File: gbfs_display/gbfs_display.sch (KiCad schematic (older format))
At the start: 9 parts, among them U1 esp8266_thing_dev

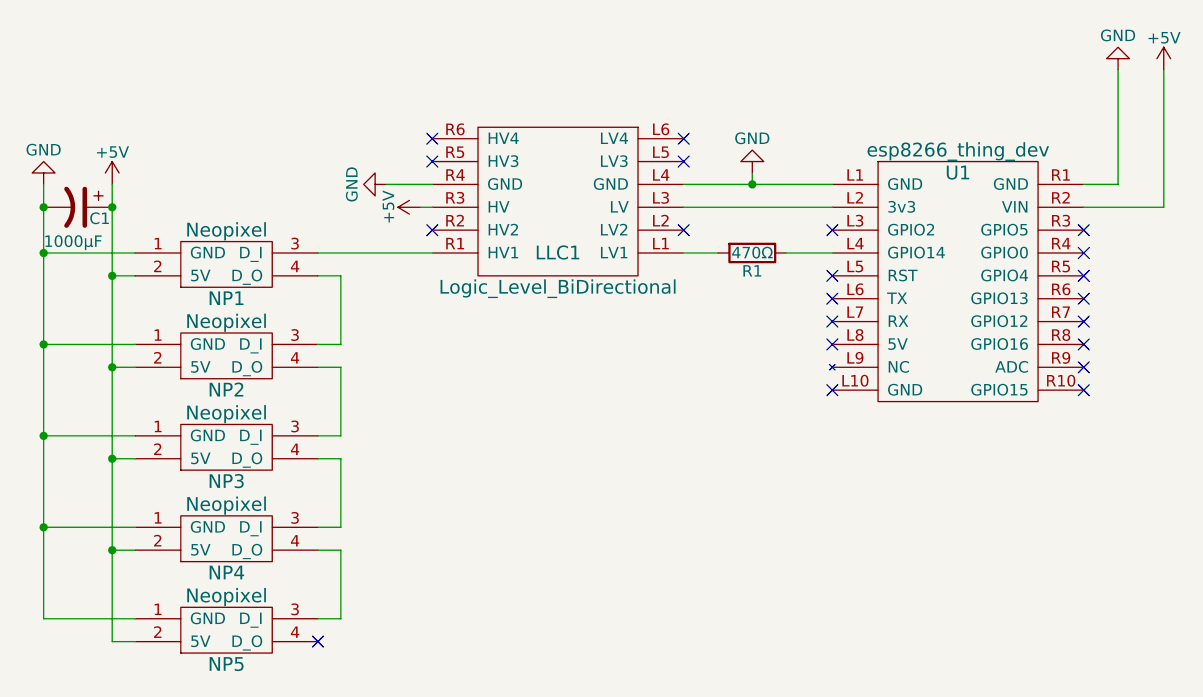
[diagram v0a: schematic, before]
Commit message: Remove neopixels and add footprints
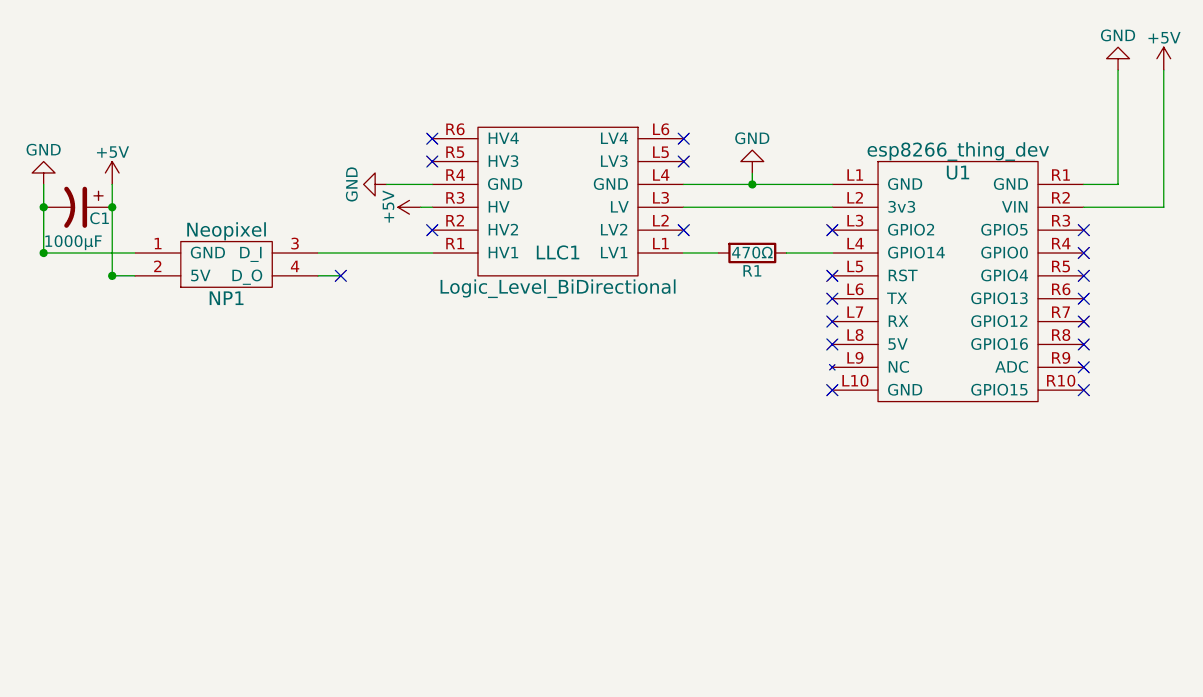
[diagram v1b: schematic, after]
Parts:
- removed NP2, NP3, NP4, NP5: Neopixel, symbol Neopixel
- C1: footprint (none) -> Capacitors_ThroughHole:CP_Radial_D10.0mm_P5.00mm
- LLC1: footprint (none) -> gbfs_display:Logic_Level_Bidirectional
- NP1: footprint (none) -> Wire_Pads:SolderWirePad_3x_2-5mmDrill
- R1: footprint (none) -> Resistors_ThroughHole:R_Axial_DIN0204_L3.6mm_D1.6mm_P5.08mm_Horizontal
- U1: footprint (none) -> gbfs_display:esp8266_thing
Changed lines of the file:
@@
 F 0 "U1" H 6050 3350 60  0000 C CNN
 F 1 "esp8266_thing_dev" H 6050 3450 60  0000 C CNN
-F 2 "" H 6050 2750 60  0001 C CNN
+F 2 "gbfs_display:esp8266_thing" H 6050 2750 60  0001 C CNN
 F 3 "" H 6050 2750 60  0001 C CNN
 	1    6050 2850
@@
 F 0 "LLC1" H 4300 2700 60  0000 C CNN
 F 1 "Logic_Level_BiDirectional" H 4300 2850 60  0000 C CNN
-F 2 "" H 4300 2150 60  0001 C CNN
+F 2 "gbfs_display:Logic_Level_Bidirectional" H 4300 2150 60  0001 C CNN
 F 3 "" H 4300 2150 60  0001 C CNN
 	1    4300 2250
@@
 F 0 "NP1" H 2850 3400 60  0000 C CNN
 F 1 "Neopixel" H 2850 3700 60  0000 C CNN
-F 2 "" H 2850 3050 60  0001 C CNN
+F 2 "Wire_Pads:SolderWirePad_3x_2-5mmDrill" H 2850 3050 60  0001 C CNN
 F 3 "" H 2850 3050 60  0001 C CNN
 	1    2850 3150
 	1    0    0    -1
 $EndComp
-$Comp
-L Neopixel NP2
-U 1 1 5A077CB3
-P 2850 3550
-F 0 "NP2" H 2850 3800 60  0000 C CNN
-F 1 "Neopixel" H 2850 4100 60  0000 C CNN
-F 2 "" H 2850 3450 60  0001 C CNN
-F 3 "" H 2850 3450 60  0001 C CNN
-	1    2850 3550
-	1    0    0    -1
-$EndComp
-$Comp
-L Neopixel NP3
-U 1 1 5A077CD9
-P 2850 3950
-F 0 "NP3" H 2850 4200 60  0000 C CNN
-F 1 "Neopixel" H 2850 4500 60  0000 C CNN
-F 2 "" H 2850 3850 60  0001 C CNN
-F 3 "" H 2850 3850 60  0001 C CNN
-	1    2850 3950
-	1    0    0    -1
-$EndComp
-$Comp
-L Neopixel NP4
-U 1 1 5A077D04
-P 2850 4350
-F 0 "NP4" H 2850 4600 60  0000 C CNN
-F 1 "Neopixel" H 2850 4900 60  0000 C CNN
-F 2 "" H 2850 4250 60  0001 C CNN
-F 3 "" H 2850 4250 60  0001 C CNN
-	1    2850 4350
-	1    0    0    -1
-$EndComp
-$Comp
-L Neopixel NP5
-U 1 1 5A077D34
-P 2850 4750
-F 0 "NP5" H 2850 5000 60  0000 C CNN
-F 1 "Neopixel" H 2850 5300 60  0000 C CNN
-F 2 "" H 2850 4650 60  0001 C CNN
-F 3 "" H 2850 4650 60  0001 C CNN
-	1    2850 4750
-	1    0    0    -1
-$EndComp
 Wire Wire Line
 	3250 2800 3350 2800
-Wire Wire Line
-	3350 2800 3350 3100
-Wire Wire Line
-	3350 3100 3250 3100
-Wire Wire Line
-	3250 3200 3350 3200
-Wire Wire Line
-	3350 3200 3350 3500
-Wire Wire Line
-	3350 3500 3250 3500
-Wire Wire Line
-	3250 3600 3350 3600
-Wire Wire Line
-	3350 3600 3350 3900
-Wire Wire Line
-	3350 3900 3250 3900
-Wire Wire Line
-	3250 4000 3350 4000
-Wire Wire Line
-	3350 4000 3350 4300
-Wire Wire Line
-	3350 4300 3250 4300
-Wire Wire Line
-	2350 3200 2450 3200
-Wire Wire Line
-	2350 3600 2450 3600
-Connection ~ 2350 3200
-Wire Wire Line
-	2350 4000 2450 4000
-Connection ~ 2350 3600
-Wire Wire Line
-	2350 4400 2450 4400
-Connection ~ 2350 4000
 Connection ~ 2350 2800
 Wire Wire Line
@@
 Wire Wire Line
 	3750 2400 3550 2400
-NoConn ~ 3250 4400
 NoConn ~ 6600 2600
 NoConn ~ 6600 2700
@@
 Wire Wire Line
 	3700 2500 3750 2500
-Wire Wire Line
-	2350 2400 2350 4400
 $Comp
 L +5V #PWR07
@@
 F 0 "C1" V 2250 2550 50  0000 L CNN
 F 1 "1000µF" V 2350 2350 50  0000 L CNN
-F 2 "" H 2200 2500 50  0000 C CNN
+F 2 "Capacitors_ThroughHole:CP_Radial_D10.0mm_P5.00mm" H 2200 2500 50  0001 C CNN
 F 3 "" H 2200 2500 50  0000 C CNN
 	1    2200 2500
 	0    1    1    0
 $EndComp
-Wire Wire Line
-	2050 2400 2050 4300
-Wire Wire Line
-	2050 4300 2450 4300
-Wire Wire Line
-	2450 3900 2050 3900
-Connection ~ 2050 3900
-Wire Wire Line
-	2450 3500 2050 3500
-Connection ~ 2050 3500
-Wire Wire Line
-	2450 3100 2050 3100
-Connection ~ 2050 3100
 Wire Wire Line
 	2450 2700 2050 2700
@@
 F 0 "R1" V 5230 2700 50  0000 C CNN
 F 1 "470Ω" V 5150 2700 50  0000 C CNN
-F 2 "" V 5080 2700 50  0000 C CNN
+F 2 "Resistors_ThroughHole:R_Axial_DIN0204_L3.6mm_D1.6mm_P5.08mm_Horizontal" V 5080 2700 50  0001 C CNN
 F 3 "" H 5150 2700 50  0000 C CNN
 	1    5150 2700
@@
 Wire Wire Line
 	5500 2500 4850 2500
+NoConn ~ 3350 2800
+Wire Wire Line
+	2350 2800 2350 2400
+Wire Wire Line
+	2050 2700 2050 2400
 $EndSCHEMATC

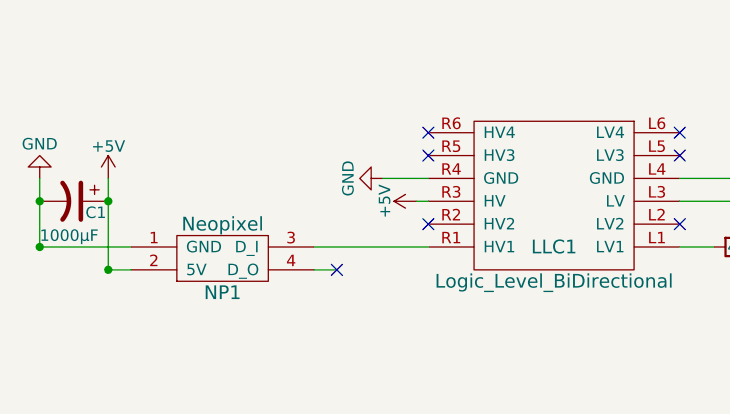
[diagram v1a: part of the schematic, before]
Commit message: New Footprint for the cable
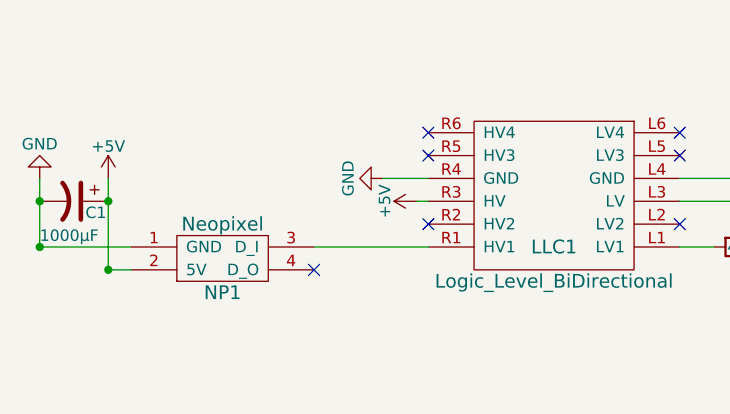
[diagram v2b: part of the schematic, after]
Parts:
- NP1: footprint Wire_Pads:SolderWirePad_3x_2-5mmDrill -> gbfs_display:NeoConnect_SolderWirePad_3x_2-5mmDrill
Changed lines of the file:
@@
 F 0 "NP1" H 2850 3400 60  0000 C CNN
 F 1 "Neopixel" H 2850 3700 60  0000 C CNN
-F 2 "Wire_Pads:SolderWirePad_3x_2-5mmDrill" H 2850 3050 60  0001 C CNN
+F 2 "gbfs_display:NeoConnect_SolderWirePad_3x_2-5mmDrill" H 2850 3050 60  0001 C CNN
 F 3 "" H 2850 3050 60  0001 C CNN
 	1    2850 3150
 	1    0    0    -1
 $EndComp
-Wire Wire Line
-	3250 2800 3350 2800
-Connection ~ 2350 2800
-Wire Wire Line
-	3750 2700 3250 2700
-Wire Wire Line
-	6750 1900 6750 2400
-Wire Wire Line
-	6750 2400 6600 2400
-Wire Wire Line
-	3750 2400 3550 2400
 NoConn ~ 6600 2600
 NoConn ~ 6600 2700
@@
 	-1   0    0    1
 $EndComp
-Connection ~ 5150 2400
-Wire Wire Line
-	6600 2500 6950 2500
-Wire Wire Line
-	6950 2500 6950 1900
-Wire Wire Line
-	2450 2800 2350 2800
-Wire Wire Line
-	3700 2500 3750 2500
 $Comp
 L +5V #PWR07
@@
 	0    1    1    0
 $EndComp
-Wire Wire Line
-	2450 2700 2050 2700
-Connection ~ 2050 2700
-Connection ~ 2050 2500
-Connection ~ 2350 2500
 $Comp
 L R R1
@@
 $EndComp
 Wire Wire Line
-	5500 2400 4850 2400
+	2050 2700 2050 2400
+Wire Wire Line
+	2350 2800 2350 2400
+Wire Wire Line
+	5500 2500 4850 2500
+Wire Wire Line
+	5000 2700 4850 2700
+Wire Wire Line
+	5500 2700 5300 2700
 Wire Wire Line
 	5150 2350 5150 2400
 Wire Wire Line
-	5500 2700 5300 2700
+	5500 2400 4850 2400
+Connection ~ 2350 2500
+Connection ~ 2050 2500
+Connection ~ 2050 2700
 Wire Wire Line
-	5000 2700 4850 2700
+	2450 2700 2050 2700
 Wire Wire Line
-	5500 2500 4850 2500
-NoConn ~ 3350 2800
+	3700 2500 3750 2500
 Wire Wire Line
-	2350 2800 2350 2400
+	2450 2800 2350 2800
 Wire Wire Line
-	2050 2700 2050 2400
+	6950 2500 6950 1900
+Wire Wire Line
+	6600 2500 6950 2500
+Connection ~ 5150 2400
+Wire Wire Line
+	3750 2400 3550 2400
+Wire Wire Line
+	6750 2400 6600 2400
+Wire Wire Line
+	6750 1900 6750 2400
+Wire Wire Line
+	3750 2700 3250 2700
+Connection ~ 2350 2800
+NoConn ~ 3250 2800
 $EndSCHEMATC

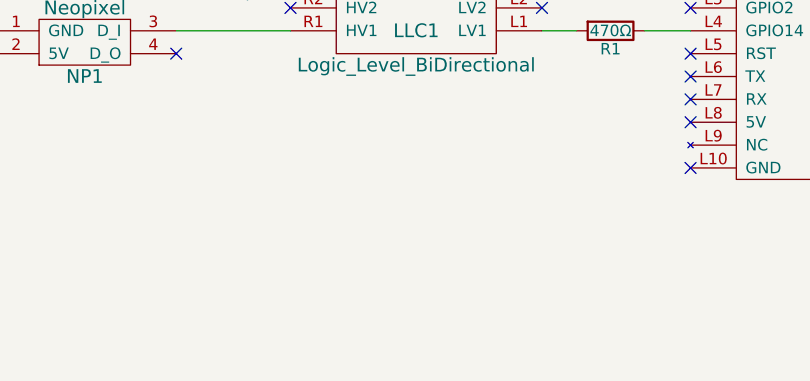
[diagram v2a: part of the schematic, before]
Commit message: Add power to schematic
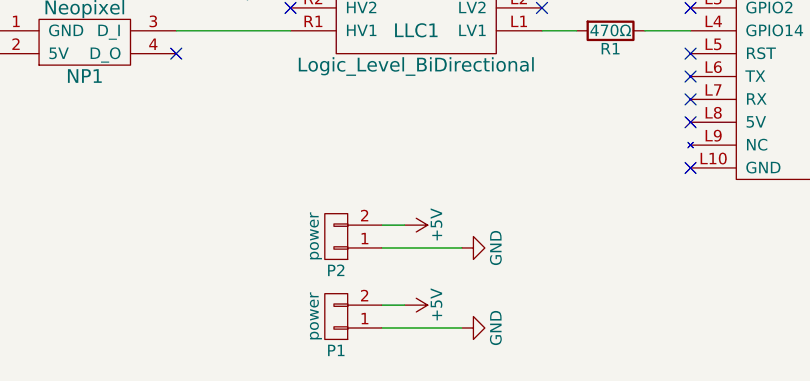
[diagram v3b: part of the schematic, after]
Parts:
- added P1, P2: power, symbol aux_conn
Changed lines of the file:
@@
 LIBS:valves
 LIBS:gbfs_lib
+LIBS:gbfs_display-cache
 EELAYER 25 0
 EELAYER END
@@
 Connection ~ 2350 2800
 NoConn ~ 3250 2800
+$Comp
+L aux_conn P1
+U 1 1 5A07C2BB
+P 3950 3950
+F 0 "P1" H 3950 4100 50  0000 C CNN
+F 1 "power" V 4050 3950 50  0000 C CNN
+F 2 "" H 3950 3950 50  0000 C CNN
+F 3 "" H 3950 3950 50  0000 C CNN
+	1    3950 3950
+	-1   0    0    1
+$EndComp
+$Comp
+L +5V #PWR?
+U 1 1 5A07C408
+P 4250 3900
+F 0 "#PWR?" H 4250 3750 50  0001 C CNN
+F 1 "+5V" H 4250 4040 50  0000 C CNN
+F 2 "" H 4250 3900 50  0000 C CNN
+F 3 "" H 4250 3900 50  0000 C CNN
+	1    4250 3900
+	0    1    1    0
+$EndComp
+$Comp
+L GND #PWR?
+U 1 1 5A07C428
+P 4500 4000
+F 0 "#PWR?" H 4500 3750 50  0001 C CNN
+F 1 "GND" H 4500 3850 50  0000 C CNN
+F 2 "" H 4500 4000 50  0000 C CNN
+F 3 "" H 4500 4000 50  0000 C CNN
+	1    4500 4000
+	0    -1   -1   0
+$EndComp
+Wire Wire Line
+	4250 3900 4150 3900
+Wire Wire Line
+	4150 4000 4500 4000
+$Comp
+L aux_conn P2
+U 1 1 5A07C552
+P 3950 3600
+F 0 "P2" H 3950 3750 50  0000 C CNN
+F 1 "power" V 4050 3600 50  0000 C CNN
+F 2 "" H 3950 3600 50  0000 C CNN
+F 3 "" H 3950 3600 50  0000 C CNN
+	1    3950 3600
+	-1   0    0    1
+$EndComp
+$Comp
+L +5V #PWR?
+U 1 1 5A07C558
+P 4250 3550
+F 0 "#PWR?" H 4250 3400 50  0001 C CNN
+F 1 "+5V" H 4250 3690 50  0000 C CNN
+F 2 "" H 4250 3550 50  0000 C CNN
+F 3 "" H 4250 3550 50  0000 C CNN
+	1    4250 3550
+	0    1    1    0
+$EndComp
+$Comp
+L GND #PWR?
+U 1 1 5A07C55E
+P 4500 3650
+F 0 "#PWR?" H 4500 3400 50  0001 C CNN
+F 1 "GND" H 4500 3500 50  0000 C CNN
+F 2 "" H 4500 3650 50  0000 C CNN
+F 3 "" H 4500 3650 50  0000 C CNN
+	1    4500 3650
+	0    -1   -1   0
+$EndComp
+Wire Wire Line
+	4250 3550 4150 3550
+Wire Wire Line
+	4150 3650 4500 3650
 $EndSCHEMATC

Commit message: Wrap up First Draft of Board
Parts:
- P1, P2: footprint (none) -> gbfs_display:Power_SolderWirePad_2x_2-5mmDrill
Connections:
- net GND: now reaches LLC1.L4 (GND), U1.L1 (GND)
- net GND: now also C1.2, LLC1.R4 (GND), NP1.1 (GND), P1.1 (P1), P2.1 (P1), U1.R1 (GND)
- net 5v: now reaches U1.R2 (VIN)
- net 5v: now also C1.1, LLC1.R3 (HV), NP1.2 (5V), P1.2 (P2), P2.2 (P2)
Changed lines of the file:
@@
 NoConn ~ 3750 2600
-$Comp
-L GND #PWR01
-U 1 1 5A079FFC
-P 6750 1900
-F 0 "#PWR01" H 6750 1650 50  0001 C CNN
-F 1 "GND" H 6750 1750 50  0000 C CNN
-F 2 "" H 6750 1900 50  0000 C CNN
-F 3 "" H 6750 1900 50  0000 C CNN
-	1    6750 1900
-	-1   0    0    1
-$EndComp
-$Comp
-L +5V #PWR02
-U 1 1 5A07A01E
-P 6950 1900
-F 0 "#PWR02" H 6950 1750 50  0001 C CNN
-F 1 "+5V" H 6950 2040 50  0000 C CNN
-F 2 "" H 6950 1900 50  0000 C CNN
-F 3 "" H 6950 1900 50  0000 C CNN
-	1    6950 1900
-	1    0    0    -1
-$EndComp
-$Comp
-L +5V #PWR03
-U 1 1 5A07A062
-P 3700 2500
-F 0 "#PWR03" H 3700 2350 50  0001 C CNN
-F 1 "+5V" H 3700 2640 50  0000 C CNN
-F 2 "" H 3700 2500 50  0000 C CNN
-F 3 "" H 3700 2500 50  0000 C CNN
-	1    3700 2500
-	0    -1   -1   0
-$EndComp
-$Comp
-L GND #PWR04
-U 1 1 5A07A08C
-P 3550 2400
-F 0 "#PWR04" H 3550 2150 50  0001 C CNN
-F 1 "GND" H 3550 2250 50  0000 C CNN
-F 2 "" H 3550 2400 50  0000 C CNN
-F 3 "" H 3550 2400 50  0000 C CNN
-	1    3550 2400
-	0    1    1    0
-$EndComp
-$Comp
-L GND #PWR05
-U 1 1 5A07A0D0
-P 2050 2400
-F 0 "#PWR05" H 2050 2150 50  0001 C CNN
-F 1 "GND" H 2050 2250 50  0000 C CNN
-F 2 "" H 2050 2400 50  0000 C CNN
-F 3 "" H 2050 2400 50  0000 C CNN
-	1    2050 2400
-	-1   0    0    1
-$EndComp
-$Comp
-L GND #PWR06
-U 1 1 5A07A0F2
-P 5150 2350
-F 0 "#PWR06" H 5150 2100 50  0001 C CNN
-F 1 "GND" H 5150 2200 50  0000 C CNN
-F 2 "" H 5150 2350 50  0000 C CNN
-F 3 "" H 5150 2350 50  0000 C CNN
-	1    5150 2350
-	-1   0    0    1
-$EndComp
-$Comp
-L +5V #PWR07
-U 1 1 5A07AABD
-P 2350 2400
-F 0 "#PWR07" H 2350 2250 50  0001 C CNN
-F 1 "+5V" H 2350 2540 50  0000 C CNN
-F 2 "" H 2350 2400 50  0000 C CNN
-F 3 "" H 2350 2400 50  0000 C CNN
-	1    2350 2400
-	1    0    0    -1
-$EndComp
 $Comp
 L CP1 C1
@@
 F 0 "P1" H 3950 4100 50  0000 C CNN
 F 1 "power" V 4050 3950 50  0000 C CNN
-F 2 "" H 3950 3950 50  0000 C CNN
+F 2 "gbfs_display:Power_SolderWirePad_2x_2-5mmDrill" H 3950 3950 50  0001 C CNN
 F 3 "" H 3950 3950 50  0000 C CNN
 	1    3950 3950
 	-1   0    0    1
-$EndComp
-$Comp
-L +5V #PWR?
-U 1 1 5A07C408
-P 4250 3900
-F 0 "#PWR?" H 4250 3750 50  0001 C CNN
-F 1 "+5V" H 4250 4040 50  0000 C CNN
-F 2 "" H 4250 3900 50  0000 C CNN
-F 3 "" H 4250 3900 50  0000 C CNN
-	1    4250 3900
-	0    1    1    0
-$EndComp
-$Comp
-L GND #PWR?
-U 1 1 5A07C428
-P 4500 4000
-F 0 "#PWR?" H 4500 3750 50  0001 C CNN
-F 1 "GND" H 4500 3850 50  0000 C CNN
-F 2 "" H 4500 4000 50  0000 C CNN
-F 3 "" H 4500 4000 50  0000 C CNN
-	1    4500 4000
-	0    -1   -1   0
 $EndComp
 Wire Wire Line
@@
 F 0 "P2" H 3950 3750 50  0000 C CNN
 F 1 "power" V 4050 3600 50  0000 C CNN
-F 2 "" H 3950 3600 50  0000 C CNN
+F 2 "gbfs_display:Power_SolderWirePad_2x_2-5mmDrill" H 3950 3600 50  0001 C CNN
 F 3 "" H 3950 3600 50  0000 C CNN
 	1    3950 3600
 	-1   0    0    1
-$EndComp
-$Comp
-L +5V #PWR?
-U 1 1 5A07C558
-P 4250 3550
-F 0 "#PWR?" H 4250 3400 50  0001 C CNN
-F 1 "+5V" H 4250 3690 50  0000 C CNN
-F 2 "" H 4250 3550 50  0000 C CNN
-F 3 "" H 4250 3550 50  0000 C CNN
-	1    4250 3550
-	0    1    1    0
-$EndComp
-$Comp
-L GND #PWR?
-U 1 1 5A07C55E
-P 4500 3650
-F 0 "#PWR?" H 4500 3400 50  0001 C CNN
-F 1 "GND" H 4500 3500 50  0000 C CNN
-F 2 "" H 4500 3650 50  0000 C CNN
-F 3 "" H 4500 3650 50  0000 C CNN
-	1    4500 3650
-	0    -1   -1   0
 $EndComp
 Wire Wire Line
@@
 Wire Wire Line
 	4150 3650 4500 3650
+Text Label 4500 3650 0    60   ~ 0
+GND
+Text Label 2050 2400 1    60   ~ 0
+GND
+Text Label 5150 2350 1    60   ~ 0
+GND
+Text Label 6750 1900 1    60   ~ 0
+GND
+Text Label 3550 2400 2    60   ~ 0
+GND
+Text Label 4500 4000 0    60   ~ 0
+GND
+Text Label 6950 1900 1    60   ~ 0
+5v
+Text Label 3700 2500 2    60   ~ 0
+5v
+Text Label 4250 3550 0    60   ~ 0
+5v
+Text Label 4250 3900 0    60   ~ 0
+5v
+Text Label 2350 2400 1    60   ~ 0
+5v
 $EndSCHEMATC

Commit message: Update PCB (I don't know what changed)
Committing this because it was saved - I honestly don't know what was
changed about it.
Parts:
- R1: footprint Resistors_ThroughHole:R_Axial_DIN0204_L3.6mm_D1.6mm_P5.08mm_Horizontal -> Resistors_ThroughHole:R_Axial_DIN0204_L3.6mm_D1.6mm_P7.62mm_Horizontal
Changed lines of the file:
@@
 F 0 "R1" V 5230 2700 50  0000 C CNN
 F 1 "470Ω" V 5150 2700 50  0000 C CNN
-F 2 "Resistors_ThroughHole:R_Axial_DIN0204_L3.6mm_D1.6mm_P5.08mm_Horizontal" V 5080 2700 50  0001 C CNN
+F 2 "Resistors_ThroughHole:R_Axial_DIN0204_L3.6mm_D1.6mm_P7.62mm_Horizontal" V 5080 2700 50  0001 C CNN
 F 3 "" H 5150 2700 50  0000 C CNN
 	1    5150 2700
